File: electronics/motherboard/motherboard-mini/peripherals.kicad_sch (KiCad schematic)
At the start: 11 parts, among them J2 ST1W008S4AR1500, J3 TBP02R2-381-03BE, J4 TBP02R2-381-03BE, J6 TBP02R2-381-04BE, J7 TBP02R2-381-03BE, Q3 BSS214NW

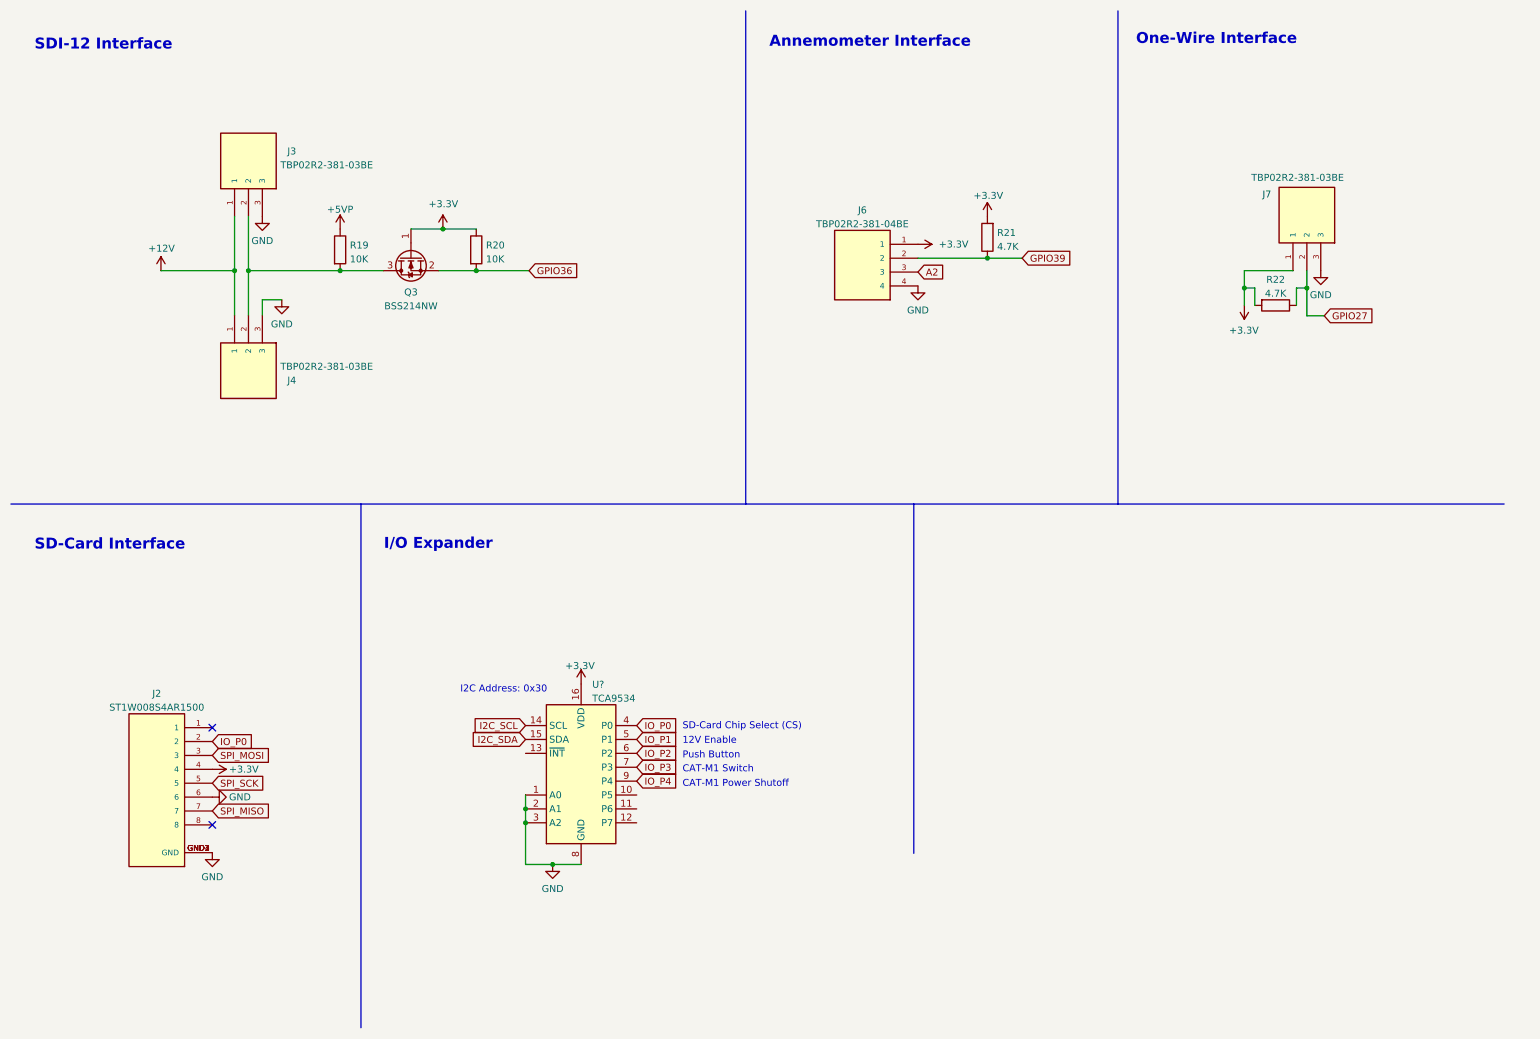
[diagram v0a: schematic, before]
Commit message: added mounting circuit board and updated motherboard for next itteration
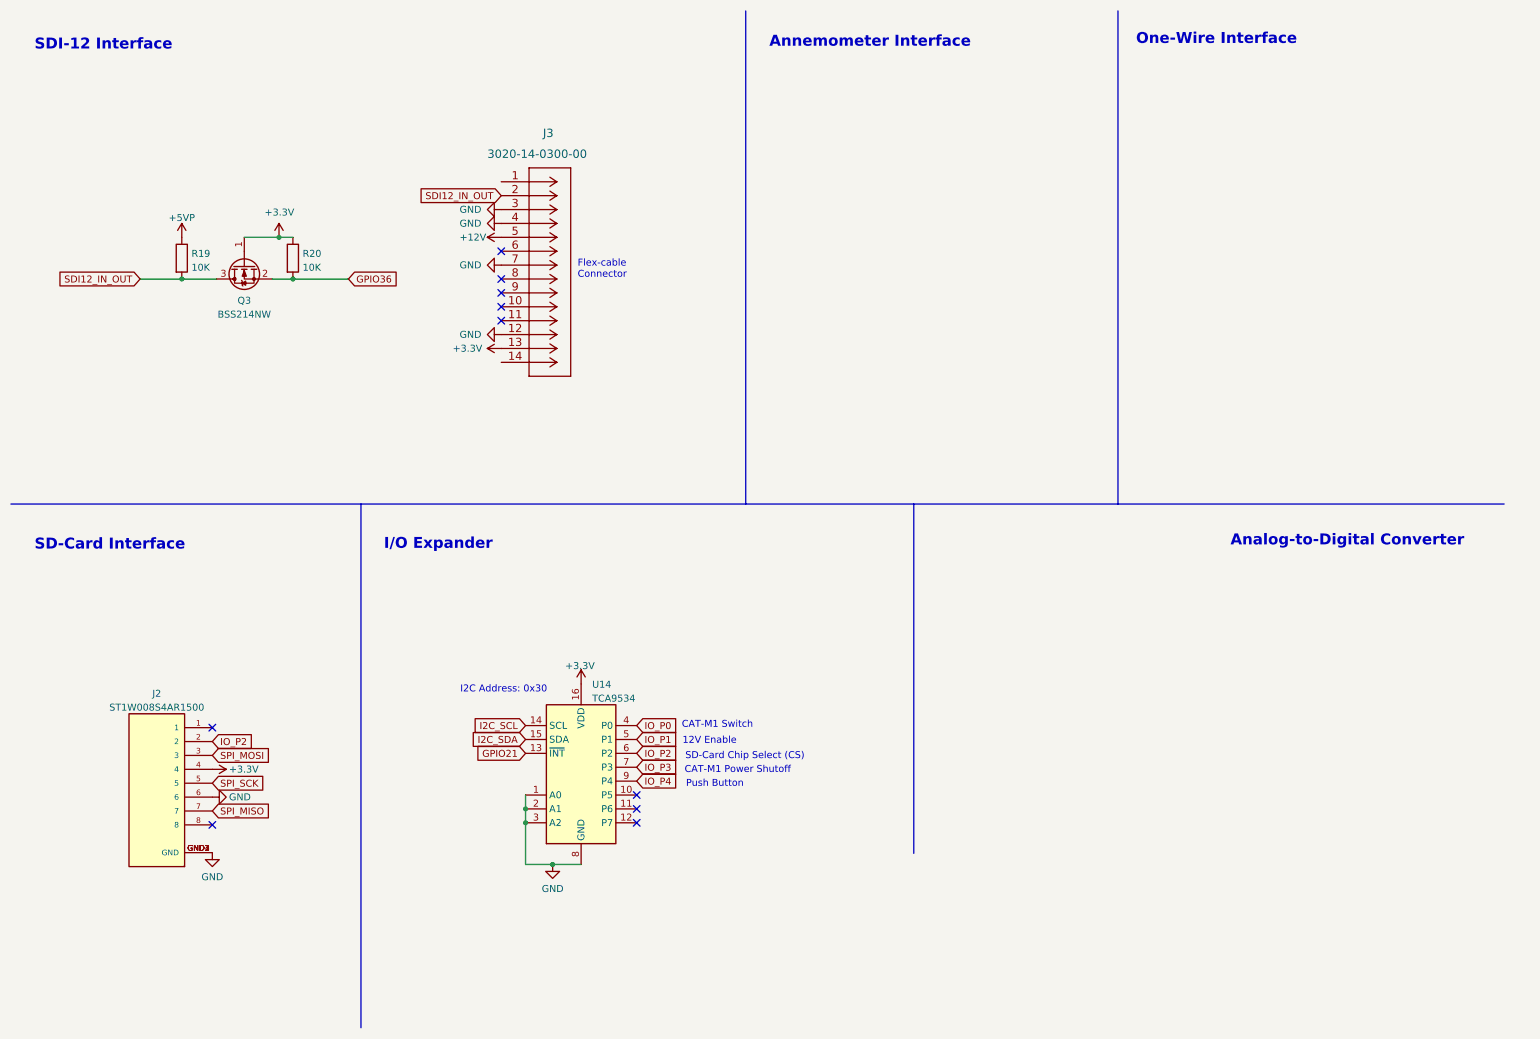
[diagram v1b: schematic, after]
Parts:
- removed J3, J4, J7: TBP02R2-381-03BE, TBP02R2-381-03BE:CUI_TBP02R2-381-03BE, symbol TBP02R2-381-03BE:TBP02R2-381-03BE
- removed J6: TBP02R2-381-04BE, TBP02R2-381-04BE:CUI_TBP02R2-381-04BE, symbol TBP02R2-381-04BE:TBP02R2-381-04BE
- removed R21, R22: 4.7K, Resistor_SMD:R_0805_2012Metric, symbol Device:R
- added J3: 3020-14-0300-00, 3020-14-0300-00:3020-14-0300-00, symbol 3020-14-0300-00:3020-14-0300-00
- U14: renamed from U?; footprint (none) -> Package_SO:TSSOP-16_4.4x5mm_P0.65mm
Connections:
- net +12V: now also J3.5
- net +3.3V: now also J3.13
- net GND: now also J3.12, J3.3, J3.4, J3.7
- net IO_P0: no longer J2.2
- net IO_P2: now also J2.2
- net SDI12_IN_OUT: now reaches Q3.3 (D), R19.2
- net SDI12_IN_OUT: now also J3.2
- net GPIO21: now reaches U14.13 (~{INT})
- no-connect marks 2 -> 10
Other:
- note added: "Analog-to-Digital Converter"
- note added: "Flex-cable Connector"
- moved on the sheet: Q3, R19, R20

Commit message: new board version sent for production, termed 'wombat' and breakout board
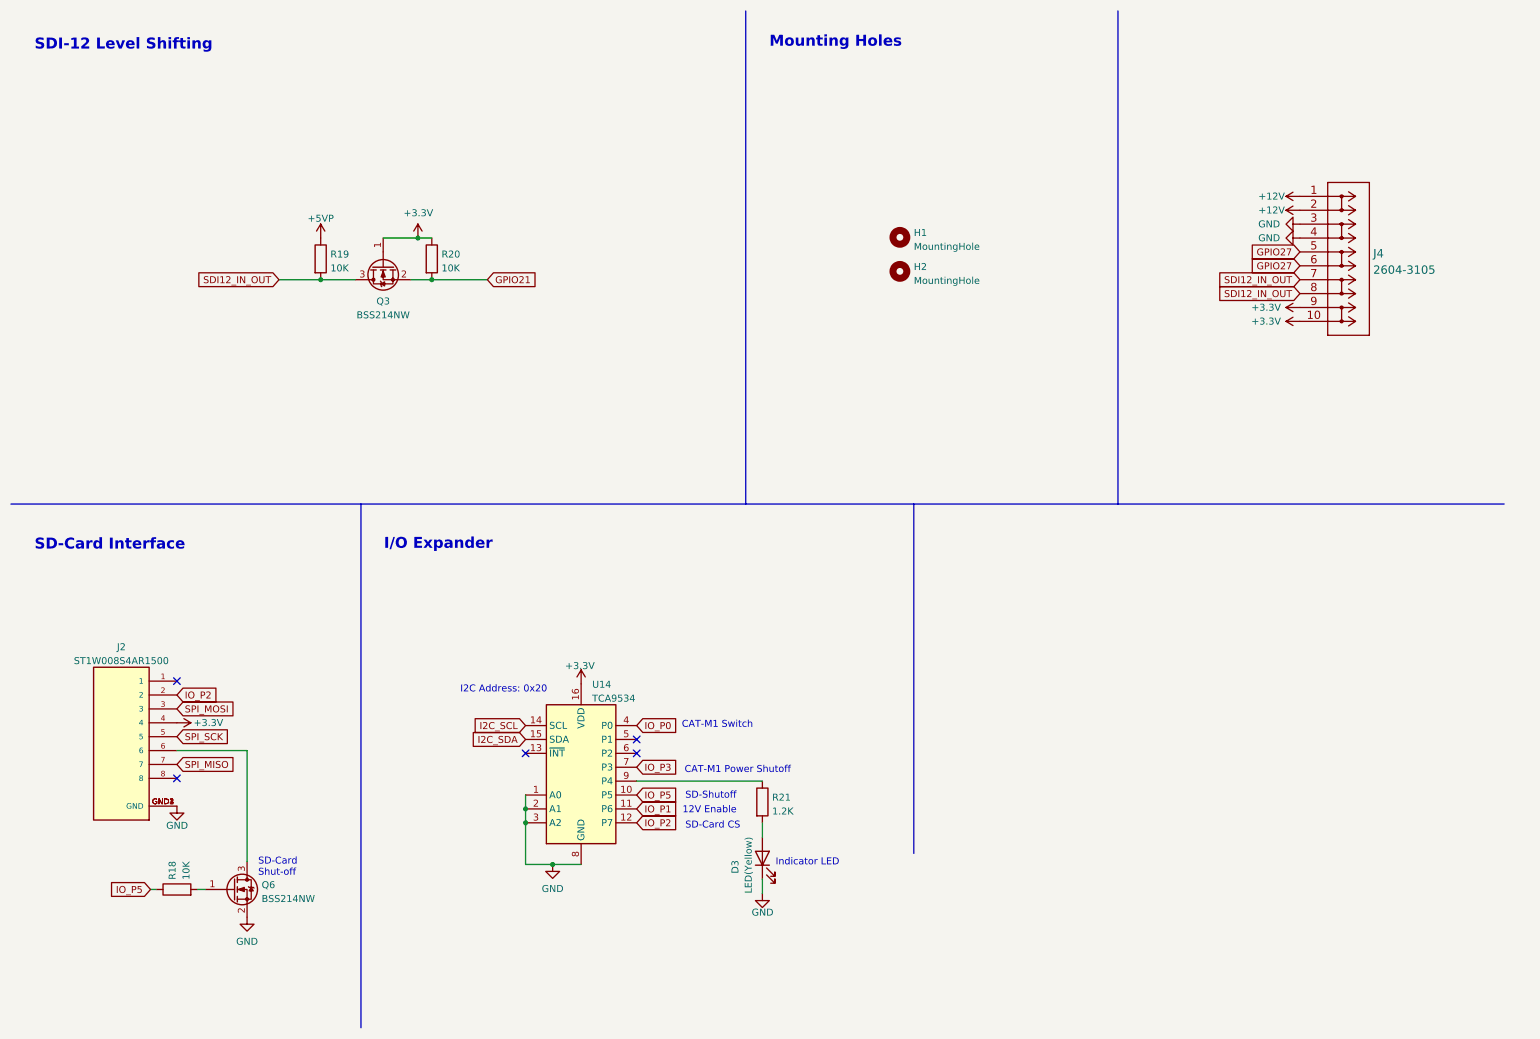
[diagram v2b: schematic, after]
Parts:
- removed J3: 3020-14-0300-00, 3020-14-0300-00:3020-14-0300-00, symbol 3020-14-0300-00:3020-14-0300-00
- added D3: LED(Yellow), LED_SMD:LED_0805_2012Metric, symbol Device:LED
- added H1, H2: MountingHole, MountingHole:MountingHole_4.3x6.2mm_M4_Pad_Via, symbol Mechanical:MountingHole
- added J4: 2604-3105, 2604-3105:2604-3105, symbol 2604-3105:2604-3105
- added Q6: BSS214NW, Package_TO_SOT_SMD:SOT-323_SC-70, symbol Transistor_FET:BSS214NW
- added R18: 10K, Resistor_SMD:R_0805_2012Metric, symbol Device:R
- added R21: 1.2K, Resistor_SMD:R_0805_2012Metric, symbol Device:R
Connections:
- net GPIO36 is gone; now on net GPIO21: Q3.2 (S), R20.2
- net +12V: now also J4.1, J4.2
- net +3.3V: now also J4.10, J4.9
- net GND: now also D3.1 (K), J4.3, J4.4, Q6.2 (S); no longer J2.6
- net GPIO21: no longer U14.13 (~{INT})
- net IO_P1: now also U14.11 (P6); no longer U14.5 (P1)
- net IO_P2: now also U14.12 (P7); no longer U14.6 (P2)
- net SDI12_IN_OUT: now also J4.7, J4.8
- net IO_P5: now reaches U14.10 (P5)
- net IO_P5: now also R18.1
- net IO_P4: no longer names the net of U14.9 (P4)
- net IO_P4: now also R21.1
- new net: Q6.1 (G), R18.2
- new net: J2.6, Q6.3 (D)
- new net: D3.2 (A), R21.2
- new net GPIO27: J4.5, J4.6
- no-connect marks 10 -> 5
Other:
- note added: "I2C Address: 0x20"
- note added: "Indicator LED"
- note added: "Mounting Holes"
- note added: "SD-Card CS"
- note added: "SD-Card Shut-off"
- note added: "SD-Shutoff"
- note added: "SDI-12 Level Shifting"
- note removed: "Analog-to-Digital Converter"
- note removed: "Annemometer Interface"
- note removed: "Flex-cable Connector"
- note removed: "I2C Address: 0x30"
- note removed: "One-Wire Interface"
- note removed: "Push Button"
- note removed: "SD-Card Chip Select (CS)"
- note removed: "SDI-12 Interface"
- moved on the sheet: J2, Q3, R19, R20

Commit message: added component information for all items in motherboard
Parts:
- D3: value LED(Yellow) -> LED(Orange); Part (none) -> LO R976-PS-1
- J2: Part (none) -> ST1W008S4AR1500
- J4: Part (none) -> 2604-3105
- R18, R19, R20: Part (none) -> RC0805FR-0710KP
- R21: value 1.2K -> 1K
- U14: Part (none) -> TCA9534PWR
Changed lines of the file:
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@@
       (effects (font (size 1.27 1.27)) hide)
     )
-    (property "Datasheet" "http://www.ti.com/lit/ds/symlink/tca9534.pdf" (id 3) (at 118.745 152.781 0)
+    (property "Datasheet" "https://www.digikey.com.au/en/products/detail/texas-instruments/TCA9534PWR/5004966" (id 3) (at 118.745 152.781 0)
+      (effects (font (size 1.27 1.27)) hide)
+    )
+    (property "Part" "TCA9534PWR" (id 4) (at 116.205 150.241 0)
       (effects (font (size 1.27 1.27)) hide)
     )
@@
       (effects (font (size 1.27 1.27)) hide)
     )
-    (property "Datasheet" "~" (id 3) (at 88.9 57.277 0)
+    (property "Datasheet" "https://www.digikey.com.au/en/products/detail/yageo/RC0805FR-0710KP/4935334" (id 3) (at 88.9 57.277 0)
+      (effects (font (size 1.27 1.27)) hide)
+    )
+    (property "Part" "RC0805FR-0710KP" (id 4) (at 88.9 57.277 0)
       (effects (font (size 1.27 1.27)) hide)
     )
@@
       (effects (font (size 1.27 1.27)) (justify left bottom) hide)
     )
-    (property "Datasheet" "" (id 3) (at 32.131 144.653 0)
+    (property "Datasheet" "https://www.digikey.com.au/en/products/detail/jae-electronics/ST1W008S4AR1500/3720055?s=N4IgTCBcDaIMoBUCMB1ADGgHHALAQQCUkBWDEAXQF8g" (id 3) (at 32.131 144.653 0)
       (effects (font (size 1.27 1.27)) (justify left bottom) hide)
     )
@@
     (property "STANDARD" "Manufacturer Recommendations" (id 7) (at 32.131 144.653 0)
       (effects (font (size 1.27 1.27)) (justify left bottom) hide)
+    )
+    (property "Part" "ST1W008S4AR1500" (id 8) (at 32.131 144.653 0)
+      (effects (font (size 1.27 1.27)) hide)
     )
     (pin "1")
@@
       (effects (font (size 1.27 1.27)) hide)
     )
-    (property "Datasheet" "~" (id 3) (at 68.58 57.277 0)
+    (property "Datasheet" "https://www.digikey.com.au/en/products/detail/yageo/RC0805FR-0710KP/4935334" (id 3) (at 68.58 57.277 0)
+      (effects (font (size 1.27 1.27)) hide)
+    )
+    (property "Part" "RC0805FR-0710KP" (id 4) (at 68.58 57.277 0)
       (effects (font (size 1.27 1.27)) hide)
     )
@@
       (effects (font (size 1.27 1.27)) hide)
     )
-    (property "Datasheet" "~" (id 3) (at 42.291 172.593 0)
+    (property "Datasheet" "https://www.digikey.com.au/en/products/detail/yageo/RC0805FR-0710KP/4935334" (id 3) (at 42.291 172.593 0)
+      (effects (font (size 1.27 1.27)) hide)
+    )
+    (property "Part" "RC0805FR-0710KP" (id 4) (at 42.291 172.593 0)
       (effects (font (size 1.27 1.27)) hide)
     )
@@
       (effects (font (size 1.524 1.524)) hide)
     )
-    (property "Datasheet" "" (id 3) (at 257.81 56.007 0)
-      (effects (font (size 1.524 1.524)))
+    (property "Datasheet" "https://www.digikey.com.au/en/products/detail/wago-corporation/2604-3105/15551087?s=N4IgTCBcDa4GwAYAsBaAzARgQVhAXQF8g" (id 3) (at 257.81 56.007 0)
+      (effects (font (size 1.524 1.524)) hide)
+    )
+    (property "Part" "2604-3105" (id 4) (at 257.81 56.007 0)
+      (effects (font (size 1.27 1.27)) hide)
     )
     (pin "1")
@@
     (in_bom yes) (on_board yes)
     (property "Reference" "D3" (id 0) (at 144.3822 168.4655 0))
-    (property "Value" "LED(Yellow)" (id 1) (at 146.812 168.148 0))
+    (property "Value" "LED(Orange)" (id 1) (at 146.812 168.148 0))
     (property "Footprint" "LED_SMD:LED_0805_2012Metric" (id 2) (at 149.352 166.878 0)
       (effects (font (size 1.27 1.27)) hide)
     )
-    (property "Datasheet" "~" (id 3) (at 149.352 166.878 0)
+    (property "Datasheet" "https://www.digikey.com.au/en/products/detail/osram-opto-ams-osram/LO-R976-PS-1/1227955" (id 3) (at 149.352 166.878 0)
+      (effects (font (size 1.27 1.27)) hide)
+    )
+    (property "Part" "LO R976-PS-1" (id 4) (at 149.352 166.878 0)
       (effects (font (size 1.27 1.27)) hide)
     )
@@
       (effects (font (size 1.27 1.27)) (justify left))
     )
-    (property "Value" "1.2K" (id 1) (at 151.13 158.2932 0)
-      (effects (font (size 1.27 1.27)) (justify left))
-    )
+    (property "Value" "1K" (id 1) (at 151.13 158.2932 0)
+      (effects (font (size 1.27 1.27)) (justify left))
+    )

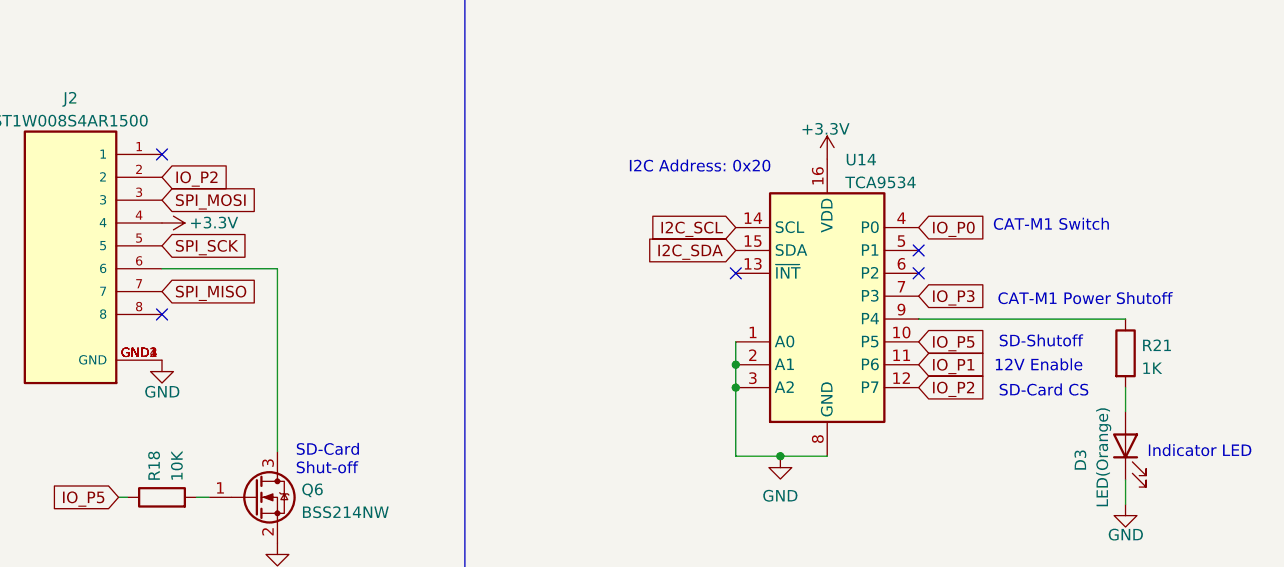
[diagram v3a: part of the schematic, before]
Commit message: updated usb-to-uart, fixed some pin label issues
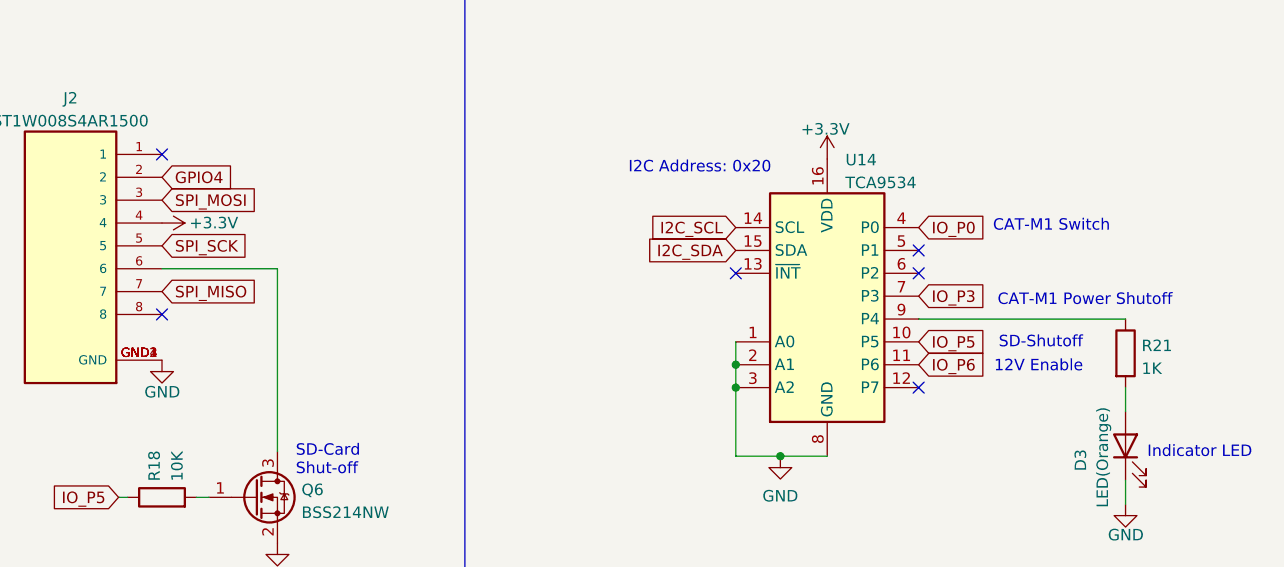
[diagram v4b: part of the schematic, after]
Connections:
- net IO_P1 renamed IO_P6
- net IO_P2: no longer names the net of U14.12 (P7)
- net IO_P2: no longer J2.2
- new net GPIO4: J2.2
- no-connect marks 5 -> 6
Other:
- note removed: "SD-Card CS"
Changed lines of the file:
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@@
   (no_connect (at 126.365 145.161))
   (no_connect (at 126.365 147.701))
+  (no_connect (at 126.365 160.401))
   (no_connect (at 42.291 152.273))
   (wire (pts (xy 126.365 152.781) (xy 149.352 152.781))
@@
     (effects (font (size 1.27 1.27)) (justify left bottom))
   )
-  (text "SD-Card CS" (at 135.255 161.671 0)
-    (effects (font (size 1.27 1.27)) (justify left bottom))
-  )
   (text "I/O Expander" (at 80.137 110.617 0)
     (effects (font (size 2 2) (thickness 0.4) bold) (justify left bottom))
@@
     (effects (font (size 1.27 1.27)) (justify left bottom))
   )
-  (global_label "IO_P2" (shape input) (at 126.365 160.401 0) (fields_autoplaced)
-    (effects (font (size 1.27 1.27)) (justify left))
-    (property "Intersheet References" "${INTERSHEET_REFS}" (id 0) (at 134.1605 160.3216 0)
-      (effects (font (size 1.27 1.27)) (justify left) hide)
-    )
-  )
   (global_label "IO_P5" (shape input) (at 37.465 172.593 180) (fields_autoplaced)
     (effects (font (size 1.27 1.27)) (justify right))
@@
     )
   )
-  (global_label "IO_P2" (shape input) (at 42.291 137.033 0) (fields_autoplaced)
-    (effects (font (size 1.27 1.27)) (justify left))
-    (property "Intersheet References" "${INTERSHEET_REFS}" (id 0) (at 50.0865 136.9536 0)
-      (effects (font (size 1.27 1.27)) (justify left) hide)
-    )
-  )
   (global_label "IO_P5" (shape input) (at 126.365 155.321 0) (fields_autoplaced)
     (effects (font (size 1.27 1.27)) (justify left))
@@
     )
   )
+  (global_label "GPIO4" (shape input) (at 42.291 137.033 0) (fields_autoplaced)
+    (effects (font (size 1.27 1.27)) (justify left))
+    (property "Intersheet References" "${INTERSHEET_REFS}" (id 0) (at 50.3889 136.9536 0)
+      (effects (font (size 1.27 1.27)) (justify left) hide)
+    )
+  )
   (global_label "SDI12_IN_OUT" (shape input) (at 247.65 61.087 180) (fields_autoplaced)
     (effects (font (size 1.27 1.27)) (justify right))
@@
     )
   )
-  (global_label "IO_P1" (shape input) (at 126.365 157.861 0) (fields_autoplaced)
+  (global_label "IO_P6" (shape input) (at 126.365 157.861 0) (fields_autoplaced)
     (effects (font (size 1.27 1.27)) (justify left))
     (property "Intersheet References" "${INTERSHEET_REFS}" (id 0) (at 134.1605 157.7816 0)
